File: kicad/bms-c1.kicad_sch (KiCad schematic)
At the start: 33 parts, among them J1 MicroFit 2x12, J2 B4B-PH-SM4, J3 USB_B_Micro, J4 B3B-PH-SM4, J5 B2B-PH-SM4, J6 B4B-PH-SM4, P1 CONN_01X01, P2 CONN_01X01, P3 CONN_01X01, P4 CONN_01X01, P5 CONN_01X01

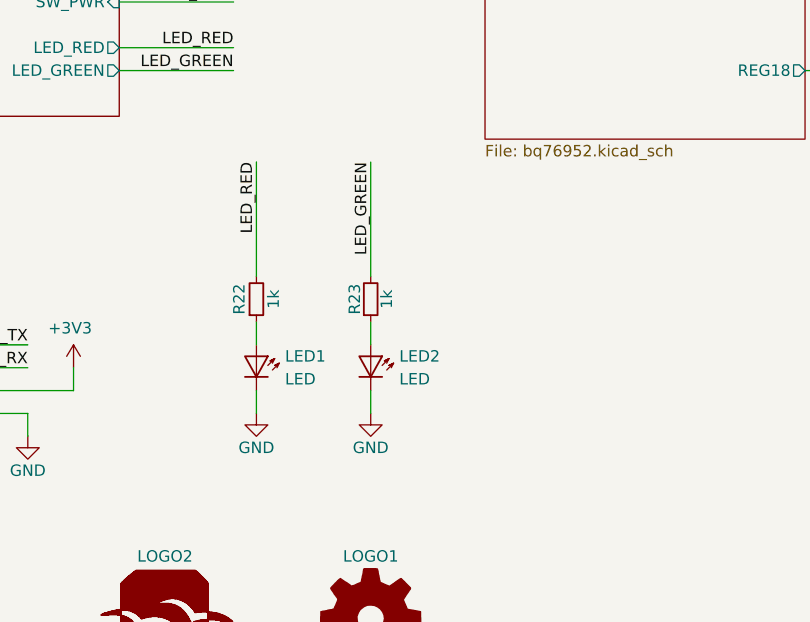
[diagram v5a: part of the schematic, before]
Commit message: All schematics on A4 and small fixes for BOM
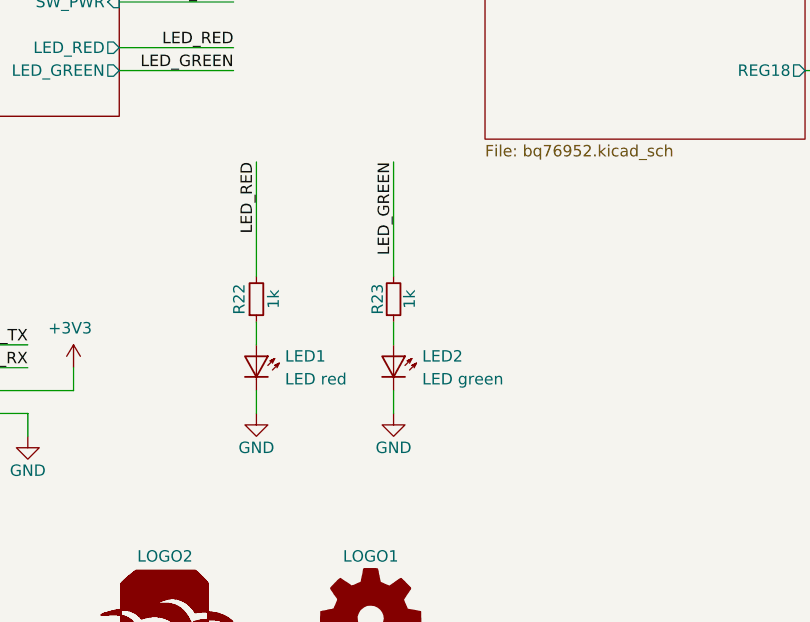
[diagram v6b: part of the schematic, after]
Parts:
- J2, J6: PartNumber (none) -> B4B-PH-SM4-TB(LF)(SN)
- J4: PartNumber (none) -> B3B-PH-SM4-TB(LF)(SN)
- J5: PartNumber (none) -> B2B-PH-SM4-TB(LF)(SN)
- LED1: value LED -> LED red
- LED2: value LED -> LED green
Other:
- moved on the sheet: LED2, R23
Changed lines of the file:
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@@
     (stroke (width 0) (type default) (color 0 0 0 0))
   )
-  (wire (pts (xy 154.94 160.02) (xy 154.94 162.56))
+  (wire (pts (xy 157.48 160.02) (xy 157.48 162.56))
     (stroke (width 0) (type default) (color 0 0 0 0))
   )
@@
     (stroke (width 0) (type default) (color 0 0 0 0))
   )
-  (wire (pts (xy 154.94 134.62) (xy 154.94 147.32))
+  (wire (pts (xy 157.48 134.62) (xy 157.48 147.32))
     (stroke (width 0) (type default) (color 0 0 0 0))
   )
@@
     (stroke (width 0) (type default) (color 0 0 0 0))
   )
-  (wire (pts (xy 154.94 152.4) (xy 154.94 154.94))
+  (wire (pts (xy 157.48 152.4) (xy 157.48 154.94))
     (stroke (width 0) (type default) (color 0 0 0 0))
   )
@@
     (effects (font (size 1.27 1.27)) (justify right bottom))
   )
-  (label "LED_GREEN" (at 154.94 134.62 270)
+  (label "LED_GREEN" (at 157.48 134.62 270)
     (effects (font (size 1.27 1.27)) (justify right bottom))
   )
@@
       (effects (font (size 1.27 1.27)) hide)
     )
+    (property "PartNumber" "B4B-PH-SM4-TB(LF)(SN)" (id 6) (at 35.56 71.12 0)
+      (effects (font (size 1.27 1.27)) hide)
+    )
     (pin "1")
     (pin "2")
@@
     )
     (property "Remarks" "Alternative: Würth 620302124022" (id 8) (at 254 109.22 0)
+      (effects (font (size 1.27 1.27)) hide)
+    )
+    (property "PartNumber" "B2B-PH-SM4-TB(LF)(SN)" (id 9) (at 254 109.22 0)
       (effects (font (size 1.27 1.27)) hide)
     )
@@
       (effects (font (size 1.27 1.27)) (justify left))
     )
-    (property "Value" "LED" (id 1) (at 145.415 158.75 0)
+    (property "Value" "LED red" (id 1) (at 145.415 158.75 0)
       (effects (font (size 1.27 1.27)) (justify left))
     )
@@
     (pin "1")
   )
-  (symbol (lib_id "power:GND") (at 154.94 162.56 0) (unit 1)
-    (in_bom yes) (on_board yes)
-    (property "Reference" "#PWR0119" (id 0) (at 154.94 168.91 0)
-      (effects (font (size 1.27 1.27)) hide)
-    )
-    (property "Value" "GND" (id 1) (at 154.94 166.37 0))
-    (property "Footprint" "" (id 2) (at 154.94 162.56 0))
-    (property "Datasheet" "" (id 3) (at 154.94 162.56 0))
+  (symbol (lib_id "power:GND") (at 157.48 162.56 0) (unit 1)
+    (in_bom yes) (on_board yes)
+    (property "Reference" "#PWR0119" (id 0) (at 157.48 168.91 0)
+      (effects (font (size 1.27 1.27)) hide)
+    )
+    (property "Value" "GND" (id 1) (at 157.48 166.37 0))
+    (property "Footprint" "" (id 2) (at 157.48 162.56 0))
+    (property "Datasheet" "" (id 3) (at 157.48 162.56 0))
     (pin "1")
   )
@@
     (pin "2")
   )
-  (symbol (lib_id "LibreSolar:R") (at 154.94 149.86 0) (mirror x) (unit 1)
-    (in_bom yes) (on_board yes)
-    (property "Reference" "R23" (id 0) (at 153.162 149.86 90))
-    (property "Value" "1k" (id 1) (at 156.718 149.86 90))
-    (property "Footprint" "LibreSolar:R_0603_1608" (id 2) (at 154.94 149.86 0)
-      (effects (font (size 1.27 1.27)) hide)
-    )
-    (property "Datasheet" "" (id 3) (at 154.94 149.86 0))
-    (property "Manufacturer" "any" (id 4) (at -106.68 25.4 0)
-      (effects (font (size 1.27 1.27)) hide)
-    )
-    (property "PartNumber" "" (id 5) (at -106.68 25.4 0)
+  (symbol (lib_id "LibreSolar:R") (at 157.48 149.86 0) (mirror x) (unit 1)
+    (in_bom yes) (on_board yes)
+    (property "Reference" "R23" (id 0) (at 155.702 149.86 90))
+    (property "Value" "1k" (id 1) (at 159.258 149.86 90))
+    (property "Footprint" "LibreSolar:R_0603_1608" (id 2) (at 157.48 149.86 0)
+      (effects (font (size 1.27 1.27)) hide)
+    )
+    (property "Datasheet" "" (id 3) (at 157.48 149.86 0))
+    (property "Manufacturer" "any" (id 4) (at -104.14 25.4 0)
+      (effects (font (size 1.27 1.27)) hide)
+    )
+    (property "PartNumber" "" (id 5) (at -104.14 25.4 0)
       (effects (font (size 1.27 1.27)) hide)
     )
@@
       (effects (font (size 1.27 1.27)) hide)
     )
+    (property "PartNumber" "B3B-PH-SM4-TB(LF)(SN)" (id 9) (at 35.56 106.68 0)
+      (effects (font (size 1.27 1.27)) hide)
+    )
     (pin "1")
     (pin "2")
@@
     (pin "1")
   )
-  (symbol (lib_id "LibreSolar:LED") (at 154.94 157.48 0) (unit 1)
-    (in_bom yes) (on_board yes)
-    (property "Reference" "LED2" (id 0) (at 158.115 156.21 0)
-      (effects (font (size 1.27 1.27)) (justify left))
-    )
-    (property "Value" "LED" (id 1) (at 158.115 158.75 0)
-      (effects (font (size 1.27 1.27)) (justify left))
-    )
-    (property "Footprint" "LED_SMD:LED_0603_1608Metric" (id 2) (at 155.575 158.75 0)
-      (effects (font (size 1.27 1.27)) hide)
-    )
-    (property "Datasheet" "" (id 3) (at 158.115 156.21 0)
-      (effects (font (size 1.27 1.27)) hide)
-    )
-    (property "Manufacturer" "any" (id 4) (at 154.94 157.48 0)
-      (effects (font (size 1.27 1.27)) hide)
-    )
-    (property "Remarks" "green" (id 5) (at 154.94 157.48 0)
+  (symbol (lib_id "LibreSolar:LED") (at 157.48 157.48 0) (unit 1)
+    (in_bom yes) (on_board yes)
+    (property "Reference" "LED2" (id 0) (at 160.655 156.21 0)
+      (effects (font (size 1.27 1.27)) (justify left))
+    )
+    (property "Value" "LED green" (id 1) (at 160.655 158.75 0)
+      (effects (font (size 1.27 1.27)) (justify left))
+    )
+    (property "Footprint" "LED_SMD:LED_0603_1608Metric" (id 2) (at 158.115 158.75 0)
+      (effects (font (size 1.27 1.27)) hide)
+    )
+    (property "Datasheet" "" (id 3) (at 160.655 156.21 0)
+      (effects (font (size 1.27 1.27)) hide)
+    )
+    (property "Manufacturer" "any" (id 4) (at 157.48 157.48 0)
+      (effects (font (size 1.27 1.27)) hide)
+    )
+    (property "Remarks" "green" (id 5) (at 157.48 157.48 0)
       (effects (font (size 1.27 1.27)) hide)
     )
@@
     )
     (property "Remarks" "Alternative: Würth 620304124022" (id 8) (at 101.6 157.48 0)
+      (effects (font (size 1.27 1.27)) hide)
+    )
+    (property "PartNumber" "B4B-PH-SM4-TB(LF)(SN)" (id 9) (at 101.6 157.48 0)
       (effects (font (size 1.27 1.27)) hide)
     )
@@
     )
     (path "/4425a08b-1c0f-41e5-a446-98dc48c5662a"
-      (reference "LED1") (unit 1) (value "LED") (footprint "LED_SMD:LED_0603_1608Metric")
+      (reference "LED1") (unit 1) (value "LED red") (footprint "LED_SMD:LED_0603_1608Metric")
     )
     (path "/adb7b528-432e-4464-9c1c-2367daa83c36"
-      (reference "LED2") (unit 1) (value "LED") (footprint "LED_SMD:LED_0603_1608Metric")
+      (reference "LED2") (unit 1) (value "LED green") (footprint "LED_SMD:LED_0603_1608Metric")
     )
     (path "/00000000-0000-0000-0000-000058f7cd5f"

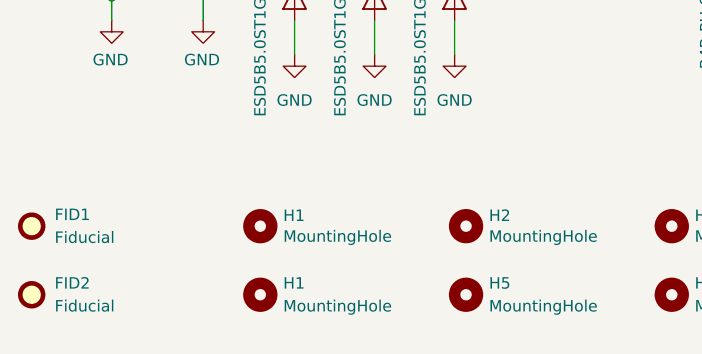
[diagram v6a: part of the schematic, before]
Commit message: v0.3.3: Final version for BMS challenge with EnAccess
Updates compared to v0.3.2:

- Optimization of some copper planes
- Net tie with thicker connection to GND
- D12 connected to Bat-

No parts were changed, the BOM is same as before.
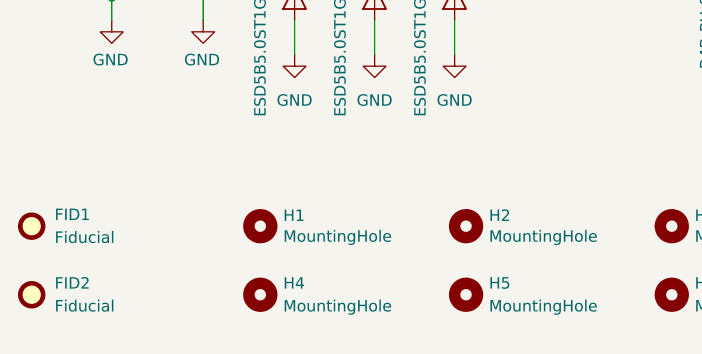
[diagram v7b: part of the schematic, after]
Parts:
- NT1: value NetTie_2 -> NetTie
- renumbered H1 to H4
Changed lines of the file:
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@@
   (title_block
     (title "Libre Solar BMS C1")
-    (date "2022-11-07")
-    (rev "0.3.2")
+    (date "2022-11-21")
+    (rev "0.3.3")
     (company "Libre Solar Technologies GmbH")
     (comment 1 "Website: https://libre.solar")
@@
     )
     (property "Datasheet" "~" (id 5) (at 254 109.22 0)
-      (effects (font (size 1.27 1.27)) hide)
-    )
-    (property "Reference" "J5" (id 6) (at 254 109.22 0)
-      (effects (font (size 1.27 1.27)) hide)
-    )
-    (property "Value" "B2B-PH-SM4" (id 7) (at 254 109.22 0)
       (effects (font (size 1.27 1.27)) hide)
     )
@@
       (effects (font (size 1.27 1.27)) hide)
     )
-    (property "Reference" "H1" (id 5) (at 48.26 187.96 0)
-      (effects (font (size 1.27 1.27)) hide)
-    )
-    (property "Value" "MountingHole" (id 6) (at 48.26 187.96 0)
-      (effects (font (size 1.27 1.27)) hide)
-    )
   )
   (symbol (lib_id "Connector_Generic:Conn_01x01") (at 73.66 55.88 0) (mirror y) (unit 1)
@@
       (effects (font (size 1.27 1.27)) hide)
     )
-    (property "Reference" "J4" (id 5) (at 35.56 106.68 0)
-      (effects (font (size 1.27 1.27)) hide)
-    )
-    (property "Value" "B3B-PH-SM4" (id 6) (at 35.56 106.68 0)
-      (effects (font (size 1.27 1.27)) hide)
-    )
     (property "Manufacturer" "JST" (id 7) (at 35.56 106.68 0)
       (effects (font (size 1.27 1.27)) hide)
@@
       (effects (font (size 1.27 1.27)) hide)
     )
-    (property "Reference" "NT1" (id 5) (at 81.28 71.12 0)
-      (effects (font (size 1.27 1.27)) hide)
-    )
-    (property "Value" "NetTie_2" (id 6) (at 81.28 71.12 0)
-      (effects (font (size 1.27 1.27)) hide)
-    )
     (pin "1")
     (pin "2")
@@
     )
     (property "Datasheet" "~" (id 4) (at 101.6 157.48 0)
-      (effects (font (size 1.27 1.27)) hide)
-    )
-    (property "Reference" "J6" (id 5) (at 101.6 157.48 0)
-      (effects (font (size 1.27 1.27)) hide)
-    )
-    (property "Value" "B4B-PH-SM4" (id 6) (at 101.6 157.48 0)
       (effects (font (size 1.27 1.27)) hide)
     )
@@
       (reference "#PWR0149") (unit 1) (value "GND") (footprint "")
     )
-    (path "/1a7f6efa-ef60-433d-acc0-6f9a9126bc57/18603329-d765-403a-ad3d-7716cc7bfb4a"
-      (reference "#PWR0150") (unit 1) (value "GND") (footprint "")
-    )
     (path "/52caf9b1-78ec-4c98-8b3e-51dda1b45836"
